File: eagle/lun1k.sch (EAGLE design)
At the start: 95 parts, among them IC1 LTC3558, IC3 STM32F405RGT, IC4 NRF24L01SMD, J2 XF2-3015-1LW, Q1 Q12M-SMD-S, Q2 3.2X2.5CRYSTAL, SW1 JS102011SAQN, SW2 SWITCH_MCTAEF, SW3 SWITCH_MCTAEF, SW4 SWITCH_MCTAEF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

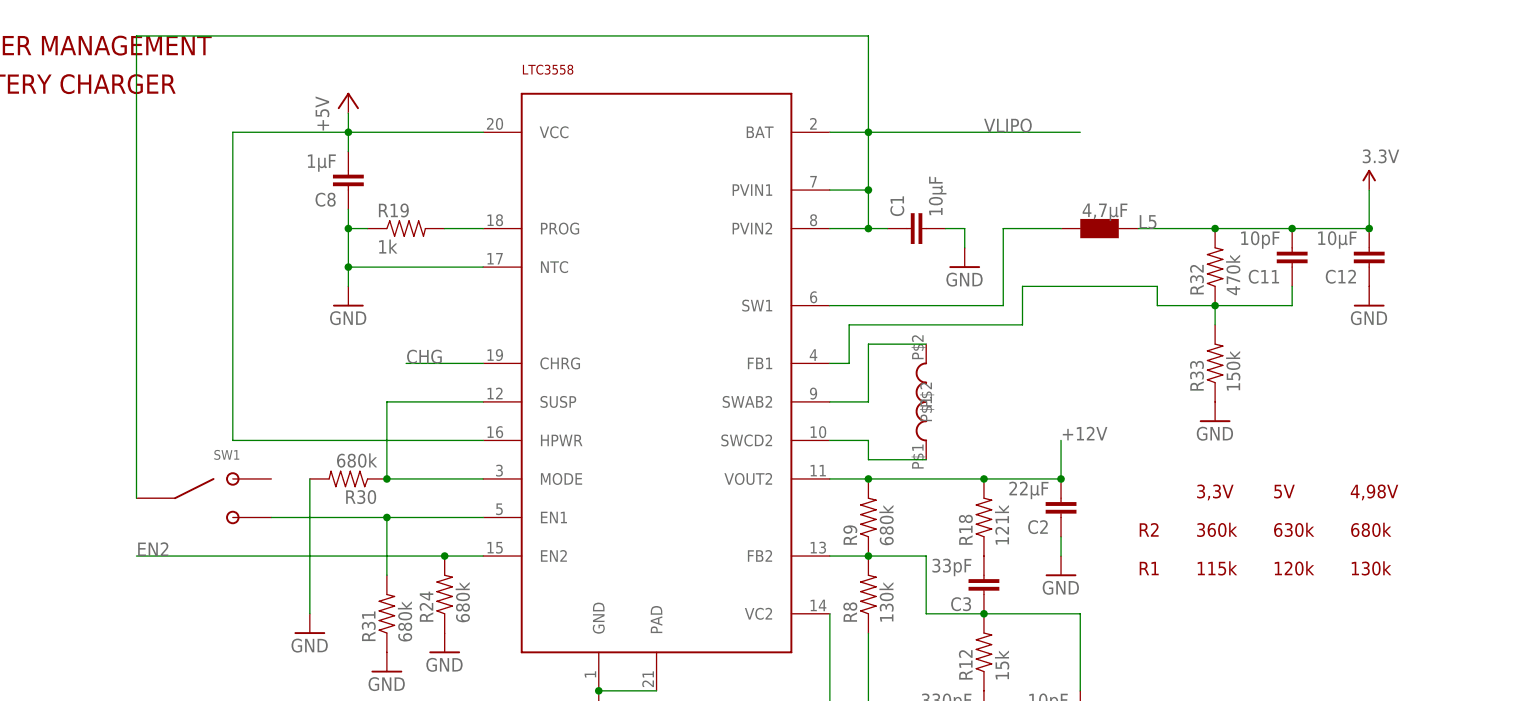
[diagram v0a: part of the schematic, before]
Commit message: switch 12V supply part 1
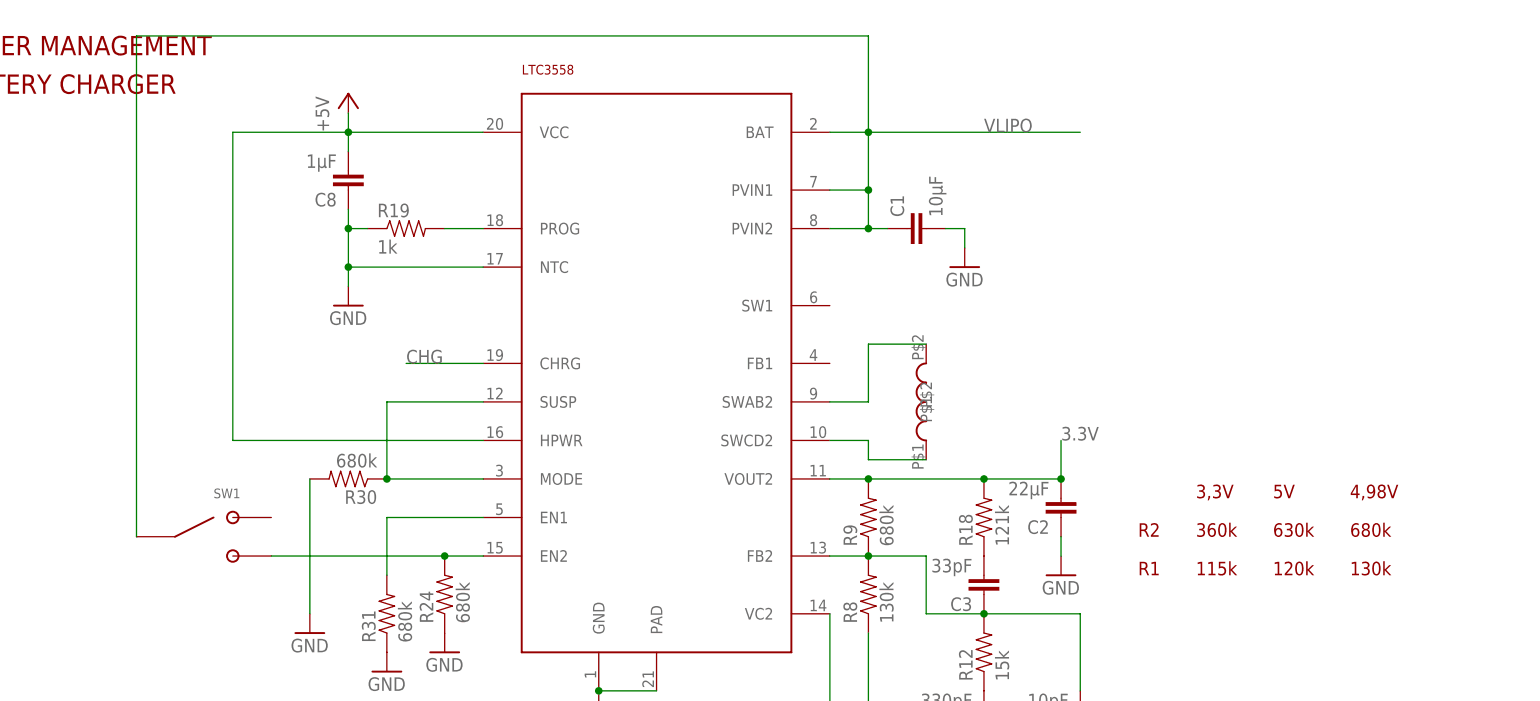
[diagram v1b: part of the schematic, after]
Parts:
- removed C11: 10pF, SparkFun:CAP0805
- removed C12: 10µF, SparkFun:CAP0805
- removed L5: 4,7µF, seb:VLF4012A
- removed R32: 470k, SparkFun-Resistors:RESISTOR0805-RES
- removed R33: 150k, SparkFun-Resistors:RESISTOR0805-RES
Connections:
- removed net N$28: C11.1, IC1.FB1, R32.1, R33.2
- removed net N$29: IC1.SW1, L5.1
- net +12V: no longer C2.2, IC1.VOUT2, R18.2, R9.2
- net 3.3V: now also C2.2, IC1.VOUT2, R18.2, R9.2; no longer C11.2, C12.2, L5.2, R32.2
- net EN2: now also SW1.3
- net GND: no longer C12.1, R33.1
- net N$27: no longer SW1.3
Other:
- moved on the sheet: SW1
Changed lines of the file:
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@@
 <part name="R31" library="SparkFun-Resistors" deviceset="RESISTOR" device="0402-RES" value="680k"/>
 <part name="GND34" library="supply1" deviceset="GND" device=""/>
-<part name="C11" library="SparkFun" deviceset="CAP" device="0805" value="10pF"/>
-<part name="R32" library="SparkFun-Resistors" deviceset="RESISTOR" device="0805-RES" value="470k"/>
-<part name="R33" library="SparkFun-Resistors" deviceset="RESISTOR" device="0805-RES" value="150k"/>
-<part name="C12" library="SparkFun" deviceset="CAP" device="0805" value="10µF"/>
-<part name="GND49" library="supply1" deviceset="GND" device=""/>
-<part name="GND50" library="supply1" deviceset="GND" device=""/>
-<part name="L5" library="seb" deviceset="VLF4012A" device="" value="4,7µF">
-<attribute name="PART" value="VLF4012A"/>
-</part>
-<part name="P+4" library="SparkFun" deviceset="3.3V" device=""/>
 <part name="P+2" library="supply1" deviceset="+5V" device=""/>
 <part name="U$1" library="seb" deviceset="RECEPTABLE_1X4_HORIZ_SMT" device=""/>
@@
 <instance part="R7" gate="G$1" x="139.7" y="226.06" rot="R90"/>
 <instance part="GND18" gate="1" x="139.7" y="215.9"/>
-<instance part="SW1" gate="SW1" x="210.82" y="200.66"/>
+<instance part="SW1" gate="SW1" x="210.82" y="195.58"/>
 <instance part="X1" gate="G$1" x="12.7" y="226.06"/>
 <instance part="FRAME1" gate="G$1" x="0" y="0"/>
@@
 <instance part="R31" gate="G$1" x="238.76" y="185.42" rot="R90"/>
 <instance part="GND34" gate="1" x="238.76" y="177.8"/>
-<instance part="C11" gate="G$1" x="358.14" y="233.68" rot="R180"/>
-<instance part="R32" gate="G$1" x="347.98" y="231.14" rot="R90"/>
-<instance part="R33" gate="G$1" x="347.98" y="218.44" rot="R90"/>
-<instance part="C12" gate="G$1" x="368.3" y="233.68" rot="R180"/>
-<instance part="GND49" gate="1" x="368.3" y="226.06"/>
-<instance part="GND50" gate="1" x="347.98" y="210.82"/>
-<instance part="L5" gate="G$1" x="332.74" y="236.22">
-<attribute name="PART" x="337.82" y="236.22" size="1.778" layer="96"/>
-</instance>
-<instance part="P+4" gate="G$1" x="368.3" y="241.3"/>
 <instance part="P+2" gate="1" x="233.68" y="254"/>
 <instance part="U$1" gate="G$1" x="353.06" y="81.28"/>
@@
 </segment>
 <segment>
-<pinref part="R33" gate="G$1" pin="1"/>
-<pinref part="GND50" gate="1" pin="GND"/>
-</segment>
-<segment>
-<pinref part="C12" gate="G$1" pin="1"/>
-<pinref part="GND49" gate="1" pin="GND"/>
-</segment>
-<segment>
 <pinref part="U1" gate="G$1" pin="ADDR"/>
 <wire x1="340.36" y1="134.62" x2="337.82" y2="134.62" width="0.1524" layer="91"/>
@@
 <pinref part="C37" gate="G$1" pin="1"/>
 <pinref part="+3V10" gate="G$1" pin="+3V3"/>
-</segment>
-<segment>
-<wire x1="347.98" y1="236.22" x2="358.14" y2="236.22" width="0.1524" layer="91"/>
-<wire x1="358.14" y1="236.22" x2="368.3" y2="236.22" width="0.1524" layer="91"/>
-<wire x1="368.3" y1="236.22" x2="368.3" y2="241.3" width="0.1524" layer="91"/>
-<wire x1="337.82" y1="236.22" x2="347.98" y2="236.22" width="0.1524" layer="91"/>
-<junction x="347.98" y="236.22"/>
-<junction x="358.14" y="236.22"/>
-<junction x="368.3" y="236.22"/>
-<pinref part="R32" gate="G$1" pin="2"/>
-<pinref part="C11" gate="G$1" pin="2"/>
-<pinref part="C12" gate="G$1" pin="2"/>
-<pinref part="L5" gate="G$1" pin="2"/>
-<pinref part="P+4" gate="G$1" pin="3.3V"/>
 </segment>
 <segment>
@@
 <pinref part="U$1" gate="G$1" pin="4@1"/>
 <junction x="353.06" y="78.74"/>
+</segment>
+<segment>
+<wire x1="297.18" y1="203.2" x2="302.26" y2="203.2" width="0.1524" layer="91"/>
+<wire x1="302.26" y1="203.2" x2="317.5" y2="203.2" width="0.1524" layer="91"/>
+<wire x1="317.5" y1="203.2" x2="327.66" y2="203.2" width="0.1524" layer="91"/>
+<wire x1="327.66" y1="203.2" x2="327.66" y2="208.28" width="0.1524" layer="91"/>
+<junction x="327.66" y="203.2"/>
+<junction x="302.26" y="203.2"/>
+<junction x="317.5" y="203.2"/>
+<pinref part="IC1" gate="G$1" pin="VOUT2"/>
+<pinref part="C2" gate="G$1" pin="2"/>
+<pinref part="R9" gate="G$1" pin="2"/>
+<pinref part="R18" gate="G$1" pin="2"/>
+<label x="327.66" y="208.28" size="1.778" layer="95"/>
 </segment>
 </net>
@@
 <label x="317.5" y="248.92" size="1.778" layer="95"/>
 <pinref part="SW1" gate="SW1" pin="2"/>
-<wire x1="205.74" y1="200.66" x2="205.74" y2="261.62" width="0.1524" layer="91"/>
+<wire x1="205.74" y1="195.58" x2="205.74" y2="261.62" width="0.1524" layer="91"/>
 <wire x1="205.74" y1="261.62" x2="302.26" y2="261.62" width="0.1524" layer="91"/>
 <wire x1="302.26" y1="261.62" x2="302.26" y2="248.92" width="0.1524" layer="91"/>
@@
 <pinref part="C30" gate="G$1" pin="+"/>
 <pinref part="J2" gate="-29" pin="MS"/>
-</segment>
-<segment>
-<wire x1="297.18" y1="203.2" x2="302.26" y2="203.2" width="0.1524" layer="91"/>
-<wire x1="302.26" y1="203.2" x2="317.5" y2="203.2" width="0.1524" layer="91"/>
-<wire x1="317.5" y1="203.2" x2="327.66" y2="203.2" width="0.1524" layer="91"/>
-<wire x1="327.66" y1="203.2" x2="327.66" y2="208.28" width="0.1524" layer="91"/>
-<junction x="327.66" y="203.2"/>
-<junction x="302.26" y="203.2"/>
-<junction x="317.5" y="203.2"/>
-<pinref part="IC1" gate="G$1" pin="VOUT2"/>
-<pinref part="C2" gate="G$1" pin="2"/>
-<pinref part="R9" gate="G$1" pin="2"/>
-<pinref part="R18" gate="G$1" pin="2"/>
-<label x="327.66" y="208.28" size="1.778" layer="95"/>
 </segment>
 </net>
@@
 <segment>
 <wire x1="251.46" y1="193.04" x2="246.38" y2="193.04" width="0.1524" layer="91"/>
-<junction x="246.38" y="193.04"/>
 <pinref part="IC1" gate="G$1" pin="EN2"/>
 <pinref part="R24" gate="G$1" pin="2"/>
-<wire x1="246.38" y1="193.04" x2="205.74" y2="193.04" width="0.1524" layer="91"/>
-<label x="205.74" y="193.04" size="1.778" layer="95"/>
+<pinref part="SW1" gate="SW1" pin="3"/>
+<wire x1="223.52" y1="193.04" x2="246.38" y2="193.04" width="0.1524" layer="91"/>
+<junction x="246.38" y="193.04"/>
 </segment>
 <segment>
@@
 <pinref part="IC1" gate="G$1" pin="EN1"/>
 <wire x1="238.76" y1="198.12" x2="251.46" y2="198.12" width="0.1524" layer="91"/>
-<wire x1="238.76" y1="198.12" x2="223.52" y2="198.12" width="0.1524" layer="91"/>
-<junction x="238.76" y="198.12"/>
-<pinref part="SW1" gate="SW1" pin="3"/>
-</segment>
-</net>
-<net name="N$28" class="0">
-<segment>
-<wire x1="322.58" y1="228.6" x2="340.36" y2="228.6" width="0.1524" layer="91"/>
-<wire x1="340.36" y1="228.6" x2="340.36" y2="226.06" width="0.1524" layer="91"/>
-<wire x1="340.36" y1="226.06" x2="347.98" y2="226.06" width="0.1524" layer="91"/>
-<wire x1="347.98" y1="226.06" x2="358.14" y2="226.06" width="0.1524" layer="91"/>
-<wire x1="358.14" y1="226.06" x2="358.14" y2="228.6" width="0.1524" layer="91"/>
-<wire x1="347.98" y1="223.52" x2="347.98" y2="226.06" width="0.1524" layer="91"/>
-<junction x="347.98" y="226.06"/>
-<pinref part="R32" gate="G$1" pin="1"/>
-<pinref part="C11" gate="G$1" pin="1"/>
-<pinref part="R33" gate="G$1" pin="2"/>
-<wire x1="322.58" y1="228.6" x2="322.58" y2="223.52" width="0.1524" layer="91"/>
-<wire x1="322.58" y1="223.52" x2="299.72" y2="223.52" width="0.1524" layer="91"/>
-<wire x1="299.72" y1="223.52" x2="299.72" y2="218.44" width="0.1524" layer="91"/>
-<pinref part="IC1" gate="G$1" pin="FB1"/>
-<wire x1="299.72" y1="218.44" x2="297.18" y2="218.44" width="0.1524" layer="91"/>
-</segment>
-</net>
-<net name="N$29" class="0">
-<segment>
-<wire x1="320.04" y1="236.22" x2="327.66" y2="236.22" width="0.1524" layer="91"/>
-<pinref part="L5" gate="G$1" pin="1"/>
-<pinref part="IC1" gate="G$1" pin="SW1"/>
-<wire x1="297.18" y1="226.06" x2="320.04" y2="226.06" width="0.1524" layer="91"/>
-<wire x1="320.04" y1="226.06" x2="320.04" y2="236.22" width="0.1524" layer="91"/>
-</segment>
-</net>
+</segment>
+</net>

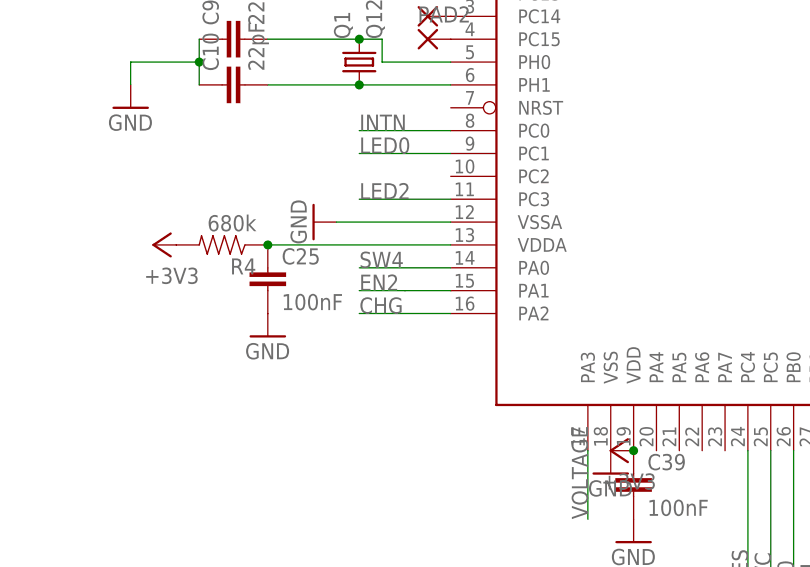
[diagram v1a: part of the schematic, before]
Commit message: switch 12V supply part 2
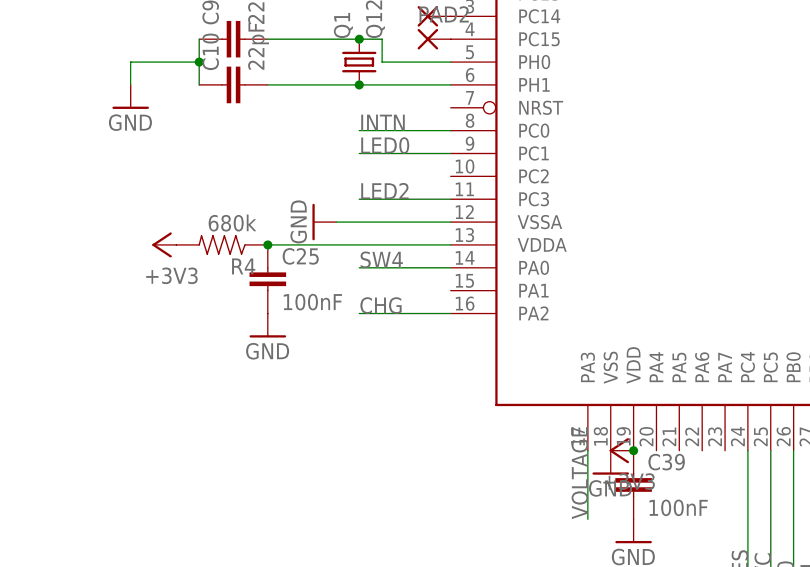
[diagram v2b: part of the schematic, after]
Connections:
- net EN2: no longer IC3.PA1
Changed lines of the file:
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@@
 <junction x="246.38" y="193.04"/>
-</segment>
-<segment>
-<label x="53.34" y="40.64" size="1.778" layer="95"/>
-<wire x1="58.42" y1="40.64" x2="53.34" y2="40.64" width="0.1524" layer="91"/>
-<pinref part="IC3" gate="G$1" pin="PA1"/>
-<wire x1="58.42" y1="40.64" x2="63.5" y2="40.64" width="0.1524" layer="91"/>
 </segment>
 </net>

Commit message: routing
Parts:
- added C11: 220pF, SparkFun:CAP0805
- added C12, C33: 1µF, SparkFun:CAP0805
- added C31, C32: 10µF, rcl:CPOL-EUSMCA
- added D1: B140F, diode:DIODE-DO214AC
- added IC2: LM27313, seb:LM27313
- added L5: 10µH, resistor:L-EUL1812
- added R11: 15k, rcl:R-EU_R0402
- added R13: 10k, SparkFun:RESISTOR0805-RES
- added R5: 100k, SparkFun:RESISTOR0805-RES
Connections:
- new net N$24: D1.A, IC2.SW, L5.2
- new net N$26: C11.2, IC2.FB, R13.2, R5.1
- new net REG_EN_: IC2./SHDN, R11.1
- net +12V: now also C11.1, C12.1, D1.C, R5.2
- net 3.3V: now also C31.+, C32.+, C33.1, IC2.IN, L5.1, R11.2
- net GND: now also C12.2, C31.-, C32.-, C33.2, IC2.GND, R13.1
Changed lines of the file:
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@@
 <part name="PAD1" library="wirepad" deviceset="SMD2" device=""/>
 <part name="PAD2" library="wirepad" deviceset="SMD2" device=""/>
+<part name="D1" library="diode" deviceset="DIODE-" device="DO214AC" value="B140F"/>
+<part name="L5" library="resistor" deviceset="L-EU" device="L1812" value="10µH"/>
+<part name="IC2" library="seb" deviceset="LM27313" device=""/>
+<part name="R5" library="SparkFun" deviceset="RESISTOR" device="0805-RES" value="100k"/>
+<part name="R13" library="SparkFun" deviceset="RESISTOR" device="0805-RES" value="10k"/>
+<part name="C11" library="SparkFun" deviceset="CAP" device="0805" value="220pF"/>
+<part name="C12" library="SparkFun" deviceset="CAP" device="0805" value="1µF"/>
+<part name="GND33" library="supply1" deviceset="GND" device=""/>
+<part name="+3V6" library="supply1" deviceset="+3V3" device=""/>
+<part name="C31" library="rcl" deviceset="CPOL-EU" device="SMCA" value="10µF"/>
+<part name="C32" library="rcl" deviceset="CPOL-EU" device="SMCA" value="10µF"/>
+<part name="C33" library="SparkFun" deviceset="CAP" device="0805" value="1µF"/>
+<part name="R11" library="rcl" deviceset="R-EU_" device="R0402" value="15k"/>
 </parts>
 <sheets>
@@
 <instance part="PAD1" gate="1" x="60.96" y="71.12"/>
 <instance part="PAD2" gate="1" x="60.96" y="68.58"/>
+<instance part="D1" gate="G$1" x="233.68" y="-25.4"/>
+<instance part="L5" gate="G$1" x="210.82" y="-25.4" rot="R90"/>
+<instance part="IC2" gate="G$1" x="210.82" y="-40.64"/>
+<instance part="R5" gate="G$1" x="243.84" y="-35.56" rot="R90"/>
+<instance part="R13" gate="G$1" x="243.84" y="-50.8" rot="R90"/>
+<instance part="C11" gate="G$1" x="251.46" y="-35.56"/>
+<instance part="C12" gate="G$1" x="261.62" y="-53.34"/>
+<instance part="GND33" gate="1" x="210.82" y="-63.5"/>
+<instance part="+3V6" gate="G$1" x="175.26" y="-22.86"/>
+<instance part="C31" gate="G$1" x="175.26" y="-40.64"/>
+<instance part="C32" gate="G$1" x="165.1" y="-40.64"/>
+<instance part="C33" gate="G$1" x="154.94" y="-43.18"/>
+<instance part="R11" gate="G$1" x="187.96" y="-43.18" rot="R90"/>
 </instances>
 <busses>
@@
 <junction x="353.06" y="86.36"/>
 </segment>
+<segment>
+<wire x1="210.82" y1="-53.34" x2="210.82" y2="-60.96" width="0.1524" layer="91"/>
+<wire x1="210.82" y1="-60.96" x2="243.84" y2="-60.96" width="0.1524" layer="91"/>
+<wire x1="243.84" y1="-60.96" x2="261.62" y2="-60.96" width="0.1524" layer="91"/>
+<wire x1="261.62" y1="-60.96" x2="261.62" y2="-55.88" width="0.1524" layer="91"/>
+<wire x1="210.82" y1="-60.96" x2="193.04" y2="-60.96" width="0.1524" layer="91"/>
+<wire x1="193.04" y1="-60.96" x2="175.26" y2="-60.96" width="0.1524" layer="91"/>
+<wire x1="175.26" y1="-60.96" x2="175.26" y2="-45.72" width="0.1524" layer="91"/>
+<wire x1="243.84" y1="-55.88" x2="243.84" y2="-60.96" width="0.1524" layer="91"/>
+<wire x1="165.1" y1="-45.72" x2="175.26" y2="-45.72" width="0.1524" layer="91"/>
+<wire x1="154.94" y1="-45.72" x2="165.1" y2="-45.72" width="0.1524" layer="91"/>
+<junction x="210.82" y="-60.96"/>
+<junction x="243.84" y="-60.96"/>
+<junction x="175.26" y="-45.72"/>
+<junction x="165.1" y="-45.72"/>
+<pinref part="IC2" gate="G$1" pin="GND"/>
+<pinref part="R13" gate="G$1" pin="1"/>
+<pinref part="C12" gate="G$1" pin="2"/>
+<pinref part="GND33" gate="1" pin="GND"/>
+<pinref part="C31" gate="G$1" pin="-"/>
+<pinref part="C32" gate="G$1" pin="-"/>
+<pinref part="C33" gate="G$1" pin="2"/>
+</segment>
 </net>
 <net name="+5V" class="1">
@@
 <pinref part="R18" gate="G$1" pin="2"/>
 <label x="327.66" y="208.28" size="1.778" layer="95"/>
+</segment>
+<segment>
+<wire x1="193.04" y1="-38.1" x2="187.96" y2="-38.1" width="0.1524" layer="91"/>
+<wire x1="187.96" y1="-38.1" x2="187.96" y2="-25.4" width="0.1524" layer="91"/>
+<wire x1="187.96" y1="-25.4" x2="205.74" y2="-25.4" width="0.1524" layer="91"/>
+<wire x1="187.96" y1="-25.4" x2="175.26" y2="-25.4" width="0.1524" layer="91"/>
+<wire x1="175.26" y1="-25.4" x2="175.26" y2="-38.1" width="0.1524" layer="91"/>
+<wire x1="165.1" y1="-38.1" x2="175.26" y2="-38.1" width="0.1524" layer="91"/>
+<wire x1="154.94" y1="-38.1" x2="165.1" y2="-38.1" width="0.1524" layer="91"/>
+<junction x="187.96" y="-25.4"/>
+<junction x="175.26" y="-25.4"/>
+<junction x="175.26" y="-38.1"/>
+<junction x="165.1" y="-38.1"/>
+<junction x="187.96" y="-38.1"/>
+<pinref part="IC2" gate="G$1" pin="IN"/>
+<pinref part="L5" gate="G$1" pin="1"/>
+<pinref part="+3V6" gate="G$1" pin="+3V3"/>
+<pinref part="C31" gate="G$1" pin="+"/>
+<pinref part="C32" gate="G$1" pin="+"/>
+<pinref part="C33" gate="G$1" pin="1"/>
+<pinref part="R11" gate="G$1" pin="2"/>
 </segment>
 </net>
@@
 <pinref part="J2" gate="-29" pin="MS"/>
 </segment>
+<segment>
+<wire x1="236.22" y1="-25.4" x2="243.84" y2="-25.4" width="0.1524" layer="91"/>
+<wire x1="243.84" y1="-25.4" x2="251.46" y2="-25.4" width="0.1524" layer="91"/>
+<wire x1="251.46" y1="-25.4" x2="261.62" y2="-25.4" width="0.1524" layer="91"/>
+<wire x1="261.62" y1="-25.4" x2="261.62" y2="-22.86" width="0.1524" layer="91"/>
+<wire x1="261.62" y1="-22.86" x2="269.24" y2="-22.86" width="0.1524" layer="91"/>
+<wire x1="261.62" y1="-25.4" x2="261.62" y2="-48.26" width="0.1524" layer="91"/>
+<wire x1="251.46" y1="-25.4" x2="251.46" y2="-30.48" width="0.1524" layer="91"/>
+<wire x1="243.84" y1="-30.48" x2="243.84" y2="-25.4" width="0.1524" layer="91"/>
+<junction x="261.62" y="-25.4"/>
+<junction x="251.46" y="-25.4"/>
+<junction x="243.84" y="-25.4"/>
+<label x="264.16" y="-22.86" size="1.778" layer="95"/>
+<pinref part="D1" gate="G$1" pin="C"/>
+<pinref part="R5" gate="G$1" pin="2"/>
+<pinref part="C11" gate="G$1" pin="1"/>
+<pinref part="C12" gate="G$1" pin="1"/>
+</segment>
 </net>
 <net name="N$14" class="0">
@@
 </segment>
 </net>
+<net name="N$24" class="0">
+<segment>
+<wire x1="215.9" y1="-25.4" x2="228.6" y2="-25.4" width="0.1524" layer="91"/>
+<wire x1="228.6" y1="-25.4" x2="231.14" y2="-25.4" width="0.1524" layer="91"/>
+<wire x1="228.6" y1="-25.4" x2="228.6" y2="-38.1" width="0.1524" layer="91"/>
+<junction x="228.6" y="-25.4"/>
+<pinref part="L5" gate="G$1" pin="2"/>
+<pinref part="D1" gate="G$1" pin="A"/>
+<pinref part="IC2" gate="G$1" pin="SW"/>
+</segment>
+</net>
+<net name="N$26" class="0">
+<segment>
+<wire x1="228.6" y1="-43.18" x2="243.84" y2="-43.18" width="0.1524" layer="91"/>
+<wire x1="243.84" y1="-43.18" x2="251.46" y2="-43.18" width="0.1524" layer="91"/>
+<wire x1="251.46" y1="-43.18" x2="251.46" y2="-38.1" width="0.1524" layer="91"/>
+<wire x1="243.84" y1="-43.18" x2="243.84" y2="-40.64" width="0.1524" layer="91"/>
+<wire x1="243.84" y1="-43.18" x2="243.84" y2="-45.72" width="0.1524" layer="91"/>
+<junction x="243.84" y="-43.18"/>
+<pinref part="IC2" gate="G$1" pin="FB"/>
+<pinref part="R5" gate="G$1" pin="1"/>
+<pinref part="R13" gate="G$1" pin="2"/>
+<pinref part="C11" gate="G$1" pin="2"/>
+</segment>
+</net>
+<net name="REG_EN_" class="0">
+<segment>
+<wire x1="187.96" y1="-48.26" x2="193.04" y2="-43.18" width="0.1524" layer="91"/>
+<pinref part="IC2" gate="G$1" pin="/SHDN"/>
+<pinref part="R11" gate="G$1" pin="1"/>
+</segment>
+</net>
